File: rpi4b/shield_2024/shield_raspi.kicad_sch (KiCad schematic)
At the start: 12 parts, among them J1 VL53, J10 LED, J11 LED, J2 LED, J3 LED, J4 Conn_02x20_Odd_Even, J5 Conn_01x04_Pin, J6 Conn_01x04_Pin, J7 VL53, J8 VL53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

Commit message: placement composant
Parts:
- added H1, H2, H3, H4: MountingHole, MountingHole:MountingHole_3.2mm_M3, symbol Mechanical:MountingHole
- added R1, R2: R, Resistor_SMD:R_0603_1608Metric, symbol Device:R
- BTN_1: renamed from J10; value LED -> BTN_1
- BTN_2: renamed from J11; value LED -> BTN_2
- LED_1: renamed from J3; value LED -> LED_1
- LED_2: renamed from J2; value LED -> LED_2
- renumbered J5 to UART_1, J6 to UART_2, J1 to VL53_1, J9 to VL53_2, J7 to VL53_3, J8 to VL53_4
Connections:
- net GPIO24 is gone; now on net BTN_1: J4.18 (Pin_18)
- net GPIO25 is gone; now on net BTN_2: J4.22 (Pin_22)
- net GND: now also R1.2, R2.2; no longer LED_1.2 (Pin_2), LED_2.2 (Pin_2)
- new net: LED_1.2 (Pin_2), R1.1
- new net: LED_2.2 (Pin_2), R2.1
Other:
- note added: "TROUS"
- moved on the sheet: LED_1, UART_1, UART_2, VL53_1, VL53_2, VL53_3, VL53_4

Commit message: routage préliminaire
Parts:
- renumbered UART_1 to UART_3, UART_2 to UART_4
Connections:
- net LED_1: now also LED_2.1 (Pin_1); no longer LED_1.1 (Pin_1)
- net LED_2: now also LED_1.1 (Pin_1); no longer LED_2.1 (Pin_1)
- net VL53_1: now also J4.35 (Pin_35); no longer J4.33 (Pin_33)
- net VL53_3: now also J4.33 (Pin_33); no longer J4.35 (Pin_35)
- net GPIO10_SDA5: no longer names the net of J4.19 (Pin_19)
- net GPIO11_SCL5: no longer names the net of J4.23 (Pin_23)
- net GPIO14_TXD0_TXD1: no longer names the net of J4.8 (Pin_8)
- net GPIO15_RXD0_RXD1: no longer names the net of J4.10 (Pin_10)
- net GPIO16: no longer names the net of J4.36 (Pin_36)
- net GPIO17: no longer names the net of J4.11 (Pin_11)
- net GPIO22_SDA6: no longer names the net of J4.15 (Pin_15)
- net GPIO23_SCL6: no longer names the net of J4.16 (Pin_16)
- net GPIO26: no longer names the net of J4.37 (Pin_37)
- net GPIO27: no longer names the net of J4.13 (Pin_13)
- net GPIO6_SDA4: no longer names the net of J4.31 (Pin_31)
- net GPIO7_SCL4: no longer names the net of J4.26 (Pin_26)
- no-connect marks 2 -> 15

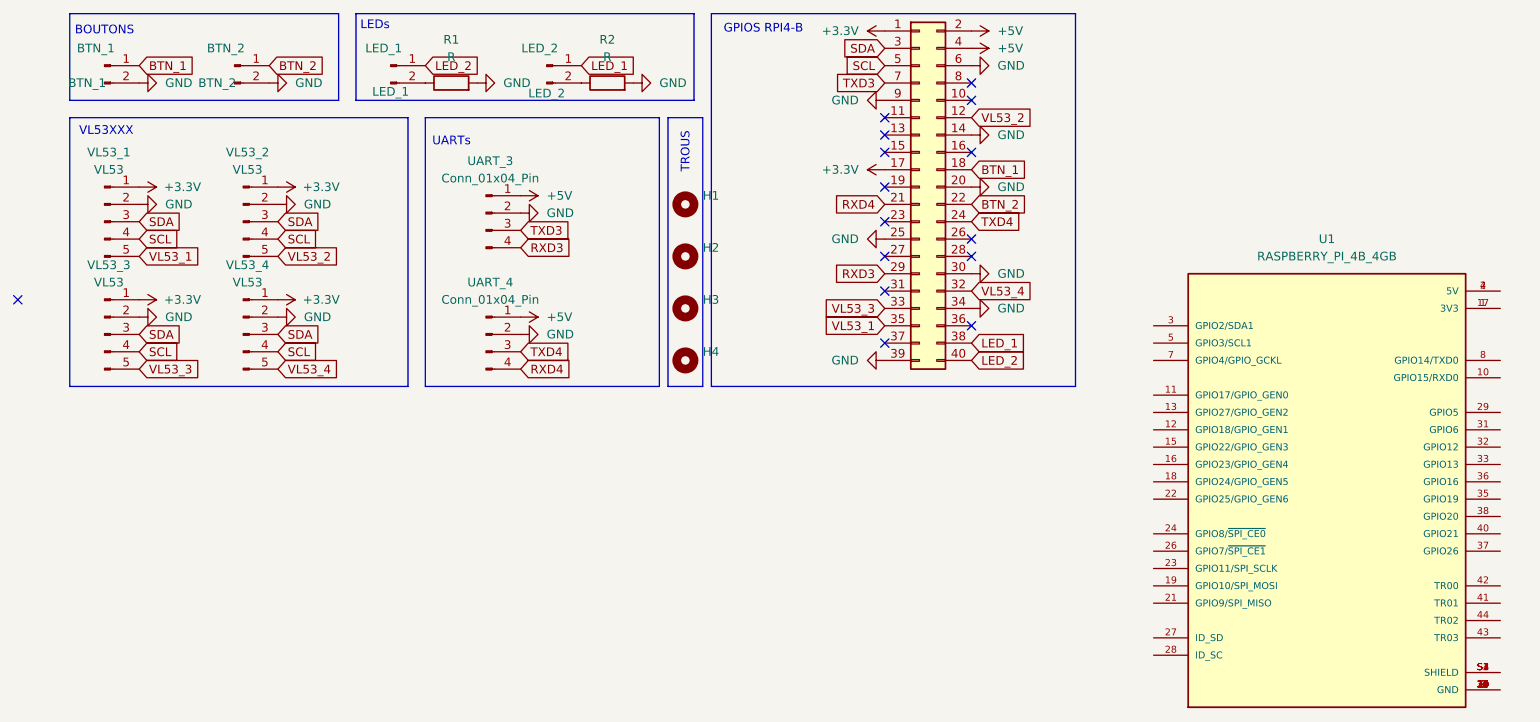
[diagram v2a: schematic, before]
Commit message: trou ventilateur + molex
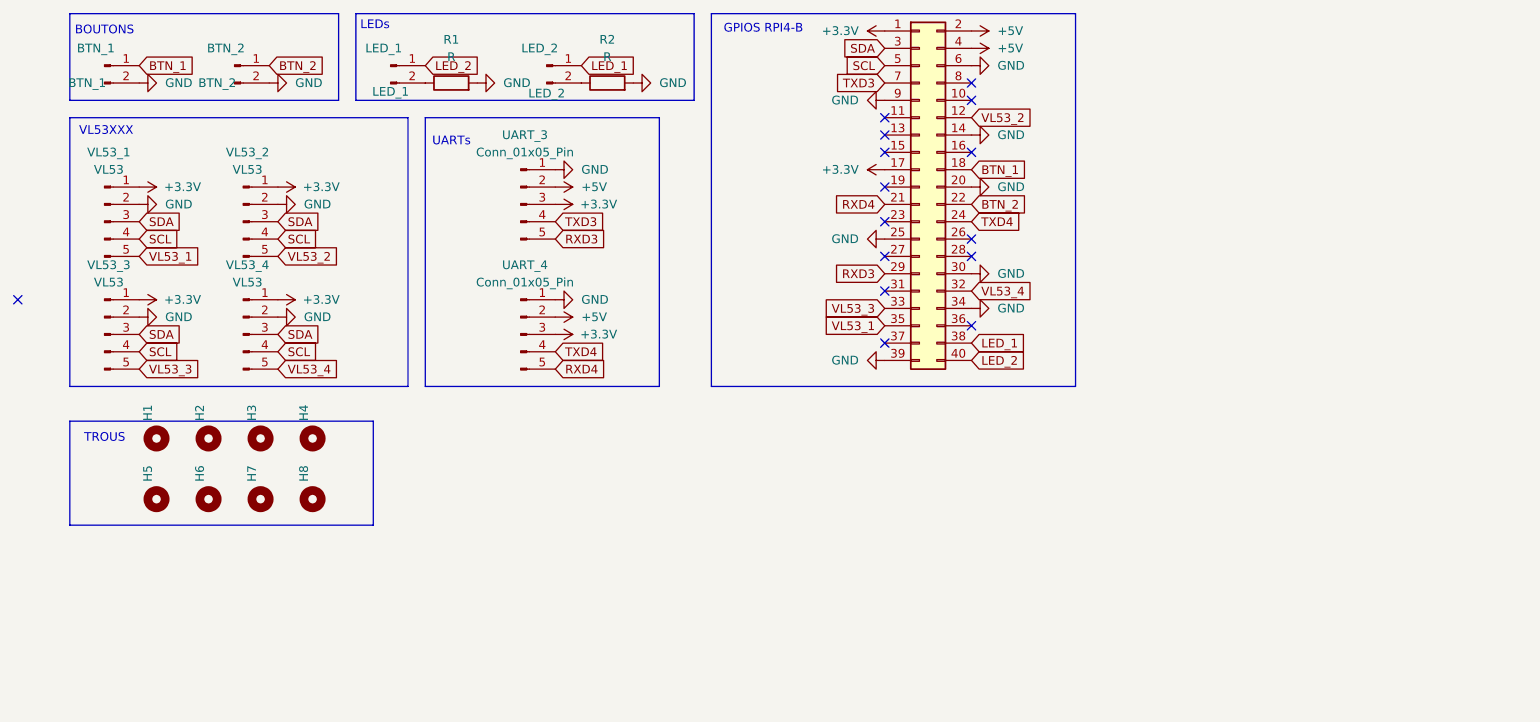
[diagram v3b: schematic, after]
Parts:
- removed U1: RASPBERRY_PI_4B_4GB, ENAC_robotique:MODULE_RASPBERRY_PI_4B_4GB, symbol ENAC_robotique:RASPBERRY_PI_4B_4GB
- removed UART_3, UART_4: Conn_01x04_Pin, Connector_PinHeader_2.54mm:PinHeader_1x04_P2.54mm_Vertical, symbol Connector:Conn_01x04_Pin
- added H5, H6, H7, H8: MountingHole, MountingHole:MountingHole_3.2mm_M3, symbol Mechanical:MountingHole
- added UART_3, UART_4: Conn_01x05_Pin, Connector_Molex:Molex_CLIK-Mate_502382-0570_1x05-1MP_P1.25mm_Vertical, symbol Connector:Conn_01x05_Pin
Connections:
- net +3.3V: now also UART_3.3 (Pin_3), UART_4.3 (Pin_3)
- net +5V: now also UART_3.2 (Pin_2), UART_4.2 (Pin_2)
- net GND: now also UART_3.1 (Pin_1), UART_4.1 (Pin_1)
- net RXD3: now also UART_3.5 (Pin_5)
- net RXD4: now also UART_4.5 (Pin_5)
- net TXD3: now also UART_3.4 (Pin_4)
- net TXD4: now also UART_4.4 (Pin_4)
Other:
- moved on the sheet: H1, H2, H3, H4

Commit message: Validation en attente + Add uarts, ventillo
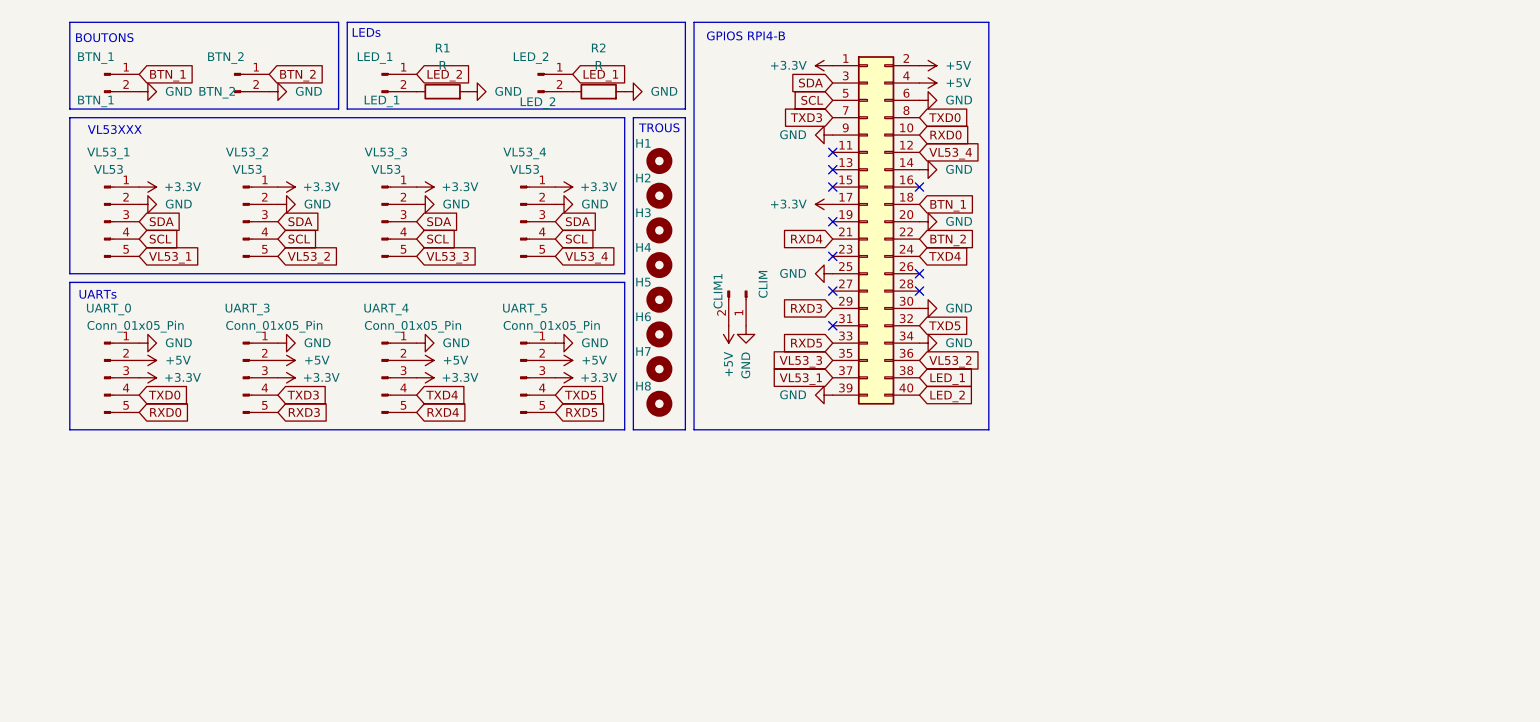
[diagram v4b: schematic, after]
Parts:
- added CLIM1: CLIM, Connector_PinHeader_2.54mm:PinHeader_1x02_P2.54mm_Vertical, symbol Connector:Conn_01x02_Pin
- added UART_0, UART_5: Conn_01x05_Pin, Connector_Molex:Molex_CLIK-Mate_502382-0570_1x05-1MP_P1.25mm_Vertical, symbol Connector:Conn_01x05_Pin
- J4: footprint Connector_PinHeader_2.54mm:PinHeader_2x20_P2.54mm_Vertical -> Connector_PinSocket_2.54mm:PinSocket_2x20_P2.54mm_Vertical
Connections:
- net +3.3V: now also UART_0.3 (Pin_3), UART_5.3 (Pin_3)
- net +5V: now also CLIM1.2 (Pin_2), UART_0.2 (Pin_2), UART_5.2 (Pin_2)
- net GND: now also CLIM1.1 (Pin_1), UART_0.1 (Pin_1), UART_5.1 (Pin_1)
- net VL53_1: now also J4.37 (Pin_37); no longer J4.35 (Pin_35)
- net VL53_2: now also J4.36 (Pin_36); no longer J4.12 (Pin_12)
- net VL53_3: now also J4.35 (Pin_35); no longer J4.33 (Pin_33)
- net VL53_4: now also J4.12 (Pin_12); no longer J4.32 (Pin_32)
- net RXD0: now reaches J4.10 (Pin_10)
- net RXD0: now also UART_0.5 (Pin_5)
- net TXD0: now reaches J4.8 (Pin_8)
- net TXD0: now also UART_0.4 (Pin_4)
- new net RXD5: J4.33 (Pin_33), UART_5.5 (Pin_5)
- new net TXD5: J4.32 (Pin_32), UART_5.4 (Pin_4)
- no-connect marks 15 -> 10
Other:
- moved on the sheet: BTN_1, BTN_2, H1, H2, H3, H4, H5, H6, H7, H8, LED_1, LED_2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

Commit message: WIP le ventillo
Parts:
- added U1: IRLML2402, myFootprints:SOT-23, symbol mySymbols:IRLML6344
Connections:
- net +5V: now also U1.3 (D); no longer CLIM1.2 (Pin_2)
- net CLIM: now reaches J4.31 (Pin_31)
- net CLIM: now also U1.1 (G)
- new net: CLIM1.2 (Pin_2), U1.2 (S)
- no-connect marks 10 -> 9
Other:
- moved on the sheet: CLIM1

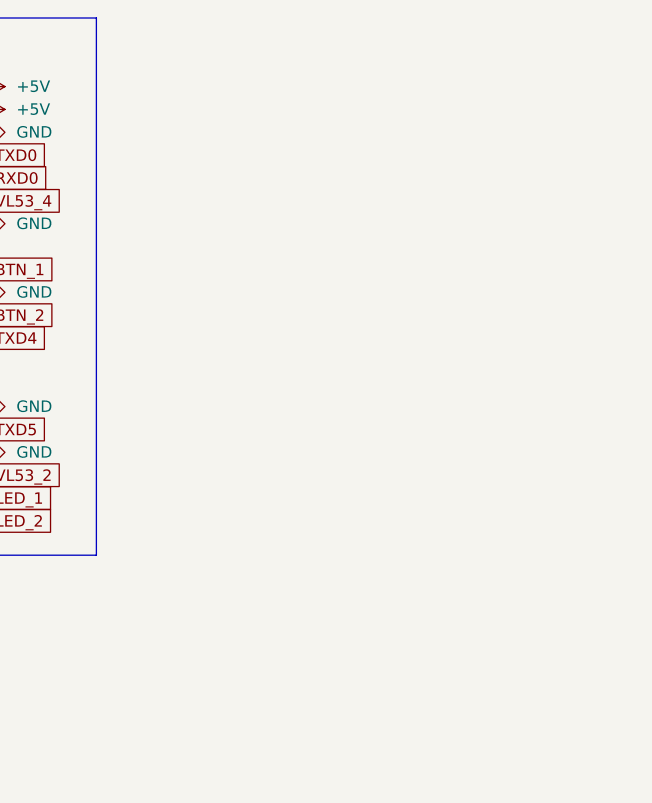
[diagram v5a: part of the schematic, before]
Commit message: ajout clim , attente de validation
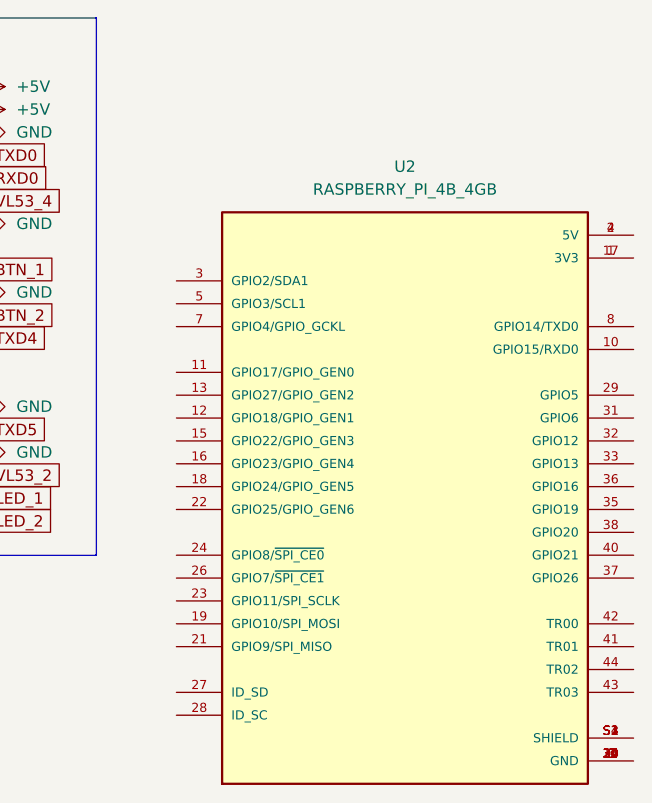
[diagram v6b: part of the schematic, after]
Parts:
- added U2: RASPBERRY_PI_4B_4GB, ENAC_robotique:MODULE_RASPBERRY_PI_4B_4GB, symbol ENAC_robotique:RASPBERRY_PI_4B_4GB
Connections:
- new net: U2.1 (3V3), U2.17 (3V3)
- new net: U2.14 (GND), U2.20 (GND), U2.25 (GND), U2.30 (GND), U2.34 (GND), U2.39 (GND), U2.6 (GND), U2.9 (GND)
- new net: U2.2 (5V), U2.4 (5V)
- new net: U2.S1 (SHIELD), U2.S2 (SHIELD), U2.S3 (SHIELD), U2.S4 (SHIELD)

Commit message: release V1
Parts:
- removed U2: RASPBERRY_PI_4B_4GB, ENAC_robotique:MODULE_RASPBERRY_PI_4B_4GB, symbol ENAC_robotique:RASPBERRY_PI_4B_4GB
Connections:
- net +5V: now also CLIM1.2 (Pin_2); no longer U1.3 (D)
- net GND: now also U1.2 (S); no longer CLIM1.1 (Pin_1)
- new net: CLIM1.1 (Pin_1), U1.3 (D)
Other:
- moved on the sheet: CLIM1

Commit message: modif avec destruction physique
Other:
- note added: "!!!!!!!!! ATTENTION !!!!!!!!! pin 35 reportée sur pin 11 ( on a coupé la piste et on a soudé un fil )"
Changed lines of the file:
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@@
 		(at 196.85 88.9)
+	)
+	(polyline
+		(pts
+			(xy 184.15 97.79) (xy 184.15 83.82)
+		)
+		(stroke
+			(width 1)
+			(type default)
+			(color 255 0 0 1)
+		)
+	)
+	(polyline
+		(pts
+			(xy 184.15 115.57) (xy 193.04 115.57)
+		)
+		(stroke
+			(width 1)
+			(type default)
+			(color 255 0 0 1)
+		)
+	)
+	(polyline
+		(pts
+			(xy 184.15 83.82) (xy 193.04 83.82)
+		)
+		(stroke
+			(width 1)
+			(type default)
+			(color 255 0 0 1)
+		)
+	)
+	(polyline
+		(pts
+			(xy 184.15 115.57) (xy 184.15 107.95)
+		)
+		(stroke
+			(width 1)
+			(type default)
+			(color 255 0 0 1)
+		)
+	)
+	(circle
+		(center 198.12 114.3)
+		(radius 2.8398)
+		(stroke
+			(width 1)
+			(type default)
+			(color 255 0 0 1)
+		)
+		(fill
+			(type none)
+		)
 	)
 	(rectangle
@@
 			(width 0)
 			(type default)
+		)
+		(fill
+			(type none)
+		)
+	)
+	(circle
+		(center 196.85 83.82)
+		(radius 2.8398)
+		(stroke
+			(width 1)
+			(type default)
+			(color 255 0 0 1)
 		)
 		(fill
@@
 		)
 	)
+	(text "!!!!!!!!! ATTENTION !!!!!!!!!\npin 35 reportée sur pin 11 \n( on a coupé la piste et \non a soudé un fil )"
+		(exclude_from_sim no)
+		(at 174.244 104.14 0)
+		(effects
+			(font
+				(size 1.27 1.27)
+				(thickness 0.254)
+				(bold yes)
+				(color 255 0 0 1)
+			)
+		)
+	)
